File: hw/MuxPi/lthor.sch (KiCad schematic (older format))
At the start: 12 parts, among them J4 CONN_01X04, J5 CONN_01X05, Q13 2N7002, Q14 2N7002, Q15 BSO130P03S, Q16 IRLML2246TRPBF, U13 TS3USB30EDGSR

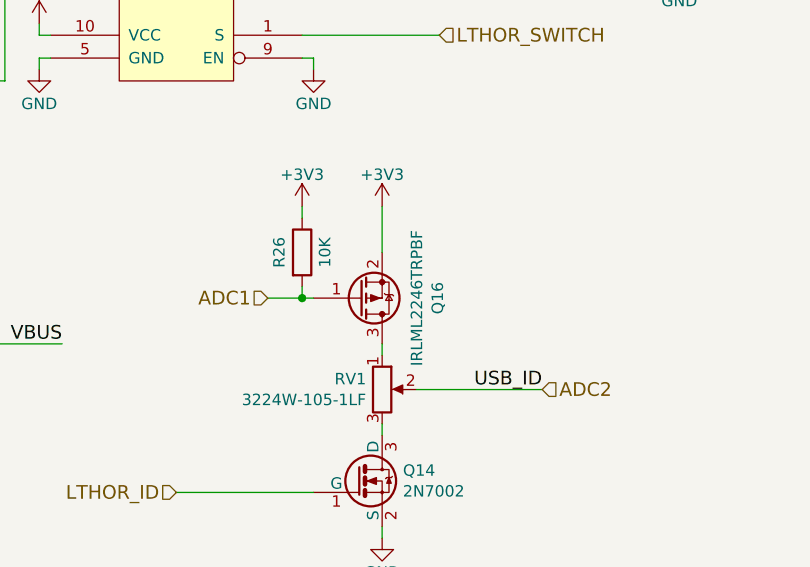
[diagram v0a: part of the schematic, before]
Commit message: Add detailed info to MuxPi electronic components
The additional information includes manufacturer names and
manufacturer symbols for all components except ceramic capacitors
and resistors. It allows to create BOM (Bill Of Materials) with
actual product names.

Change-Id: Id1c518bba60322d4b8b132ad14261806070abc27
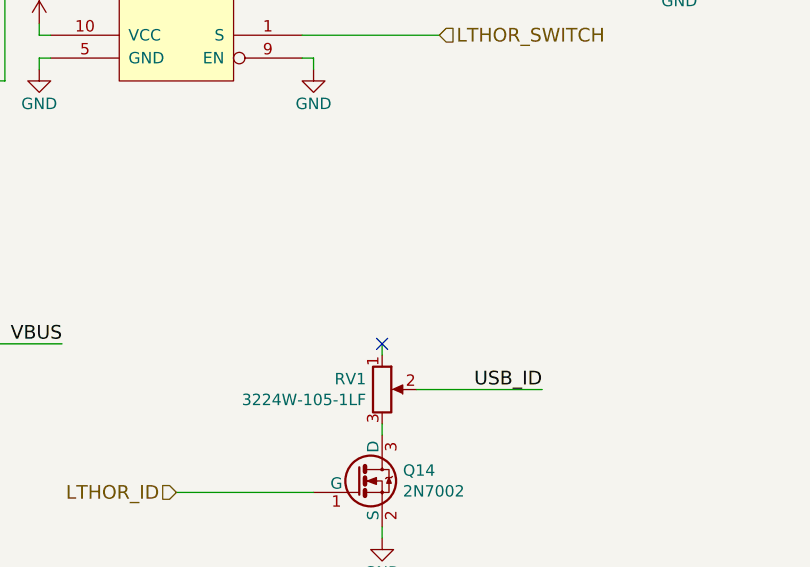
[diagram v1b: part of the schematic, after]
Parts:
- removed Q16: IRLML2246TRPBF, TO_SOT_Packages_SMD:SOT-23, symbol MuxPi:Q_PMOS_GSD
- removed R26: 10K, Resistors_SMD:R_0805, symbol MuxPi:R
- J4: Manufacturer (none) -> CONNFLY; Symbol (none) -> DS1065-01-1*4S8BV
- Q13, Q14: Manufacturer (none) -> ON SEMICONDUCTOR (FAIRCHILD); Symbol (none) -> 2N7002
- Q15: Manufacturer (none) -> INFINEON TECHNOLOGIES; Symbol (none) -> BSO130P03SHXUMA1
- RV1: Manufacturer (none) -> ALLCONNE; Symbol (none) -> POT53W105
- U13: Manufacturer (none) -> TEXAS INSTRUMENTS; Symbol (none) -> TS3USB30EDGSR
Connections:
- net ADC2 renamed USB_ID
- no-connect marks 1 -> 2
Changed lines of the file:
@@
 F 3 "http://www.tme.eu/pl/Document/cb34e048abb83f790f0df461315a2ac0/DS1065-01.pdf" H 4300 2550 50  0001 C CNN
 F 4 "http://www.tme.eu/pl/details/ds1065-01-1x4s8bv/listwy-i-gniazda-kolkowe/connfly/ds1065-01-1_4s8bv/" H 4300 2550 60  0001 C CNN "Shop link"
+F 5 "CONNFLY" H 4300 2550 50  0001 C CNN "Manufacturer"
+F 6 "DS1065-01-1*4S8BV" H 4300 2550 50  0001 C CNN "Symbol"
 	1    4300 2550
 	-1   0    0    -1
@@
 F 3 "http://www.ti.com/lit/ds/symlink/ts3usb30e.pdf" H 3690 1790 60  0001 C CNN
 F 4 "http://pl.farnell.com/texas-instruments/ts3usb30edgsr/multiplexer-demultiplexer-1-2/dp/2335701" H 5900 2900 60  0001 C CNN "Shop link"
+F 5 "TEXAS INSTRUMENTS" H 5900 2900 50  0001 C CNN "Manufacturer"
+F 6 "TS3USB30EDGSR" H 5900 2900 50  0001 C CNN "Symbol"
 	1    5900 2900
 	-1   0    0    -1
@@
 VBUS
 $Comp
-L MuxPi:2N7002 Q14
-U 1 1 58DAC98F
-P 6700 5200
-F 0 "Q14" H 6891 5246 50  0000 L CNN
-F 1 "2N7002" H 6891 5155 50  0000 L CNN
-F 2 "TO_SOT_Packages_SMD:SOT-23" H 6900 5125 50  0001 L CIN
-F 3 "https://www.nxp.com/documents/data_sheet/2N7002.pdf" H 6700 5200 50  0001 L CNN
-F 4 "http://www.tme.eu/pl/details/2n7002/tranzystory-z-kanalem-n-smd/fairchild-semiconductor/" H 6700 5200 60  0001 C CNN "Shop link"
-	1    6700 5200
-	1    0    0    -1
-$EndComp
-$Comp
 L MuxPi:GND #PWR0200
 U 1 1 58DAC996
@@
 F 3 "https://www.maritex.com.pl/product/attachment/37649/pot-53w.pdf" H 6800 4800 50  0001 C CNN
 F 4 "https://www.maritex.com.pl/elementy_pasywne/potencjometry/wieloobrotowe/wieloobrotowe_smd/potencjometry_precyzyjne_wieloobrotowe_smd/pot53w105.html" H 6800 4800 60  0001 C CNN "Shop link"
+F 5 "ALLCONNE" H 6800 4800 50  0001 C CNN "Manufacturer"
+F 6 "POT53W105" H 6800 4800 50  0001 C CNN "Symbol"
 	1    6800 4800
 	1    0    0    -1
@@
 F 3 "" H 3300 5650 60  0000 C CNN
 	1    3300 5650
-	1    0    0    -1
-$EndComp
-$Comp
-L MuxPi:BSO130P03S Q15
-U 1 1 58DAF6B4
-P 4500 4800
-F 0 "Q15" H 4500 5307 50  0000 C CNN
-F 1 "BSO130P03S" H 4500 5216 50  0000 C CNN
-F 2 "mux-footprints:SOIC-8" H 4500 5125 50  0001 C CIN
-F 3 "http://www.tme.eu/pl/Document/fde90035d9a6021d44d09086b0d9119c/BSO130P03SHXUMA1-DTE.pdf" V 4500 4800 50  0001 L CNN
-F 4 "http://www.tme.eu/pl/details/bso130p03shxuma1/tranzystory-z-kanalem-p-smd/infineon-technologies/" H 4500 4800 60  0001 C CNN "Shop link"
-	1    4500 4800
-	1    0    0    -1
-$EndComp
-$Comp
-L MuxPi:2N7002 Q13
-U 1 1 58DAF6BD
-P 3750 5200
-F 0 "Q13" H 3941 5246 50  0000 L CNN
-F 1 "2N7002" H 3941 5155 50  0000 L CNN
-F 2 "TO_SOT_Packages_SMD:SOT-23" H 3950 5125 50  0001 L CIN
-F 3 "https://www.nxp.com/documents/data_sheet/2N7002.pdf" H 3750 5200 50  0001 L CNN
-F 4 "http://www.tme.eu/pl/details/2n7002/tranzystory-z-kanalem-n-smd/fairchild-semiconductor/" H 3750 5200 60  0001 C CNN "Shop link"
-	1    3750 5200
 	1    0    0    -1
 $EndComp
@@
 Text HLabel 7050 3250 2    60   Input ~ 0
 LTHOR_SWITCH
-$Comp
-L MuxPi:Q_PMOS_GSD Q16
-U 1 1 58DB6E6E
-P 6700 4400
-F 0 "Q16" V 7043 4400 50  0000 C CNN
-F 1 "IRLML2246TRPBF" V 6952 4400 50  0000 C CNN
-F 2 "TO_SOT_Packages_SMD:SOT-23" H 6900 4500 50  0001 C CNN
-F 3 "http://www.tme.eu/pl/Document/2f0f749c8d8f8ba613dc3956fc89a382/irlml2246pbf.pdf" H 6700 4400 50  0001 C CNN
-F 4 "http://www.tme.eu/pl/details/irlml2246trpbf/tranzystory-z-kanalem-p-smd/infineon-irf/" V 6700 4400 60  0001 C CNN "Shop link"
-	1    6700 4400
-	1    0    0    1
-$EndComp
-$Comp
-L MuxPi:+3V3 #PWR199
-U 1 1 58DBC567
-P 6800 4000
-AR Path="/58DBC567" Ref="#PWR199"  Part="1"
-AR Path="/58DA42D9/58DBC567" Ref="#PWR0199"  Part="1"
-F 0 "#PWR0199" H 6800 3850 50  0001 C CNN
-F 1 "+3V3" H 6800 4140 50  0000 C CNN
-F 2 "" H 6800 4000 60  0000 C CNN
-F 3 "" H 6800 4000 60  0000 C CNN
-	1    6800 4000
-	1    0    0    -1
-$EndComp
 Wire Wire Line
 	6800 4600 6800 4650
 Wire Wire Line
-	6800 4000 6800 4200
-Wire Wire Line
-	6500 4400 6450 4400
-Text HLabel 7500 4800 2    60   Input ~ 0
-ADC2
-$Comp
-L MuxPi:R R26
-U 1 1 58DBD856
-P 6450 4200
-F 0 "R26" V 6350 4200 50  0000 C CNN
-F 1 "10K" V 6550 4200 50  0000 C CNN
-F 2 "Resistors_SMD:R_0805" V 6380 4200 30  0001 C CNN
-F 3 "" H 6450 4200 30  0000 C CNN
-F 4 "http://www.tme.eu/pl/details/smd0805-560r/rezystory-smd-0805/royal-ohm/0805s8j0561t5e/" V 6450 4200 60  0001 C CNN "Shop link"
-	1    6450 4200
-	1    0    0    -1
-$EndComp
-$Comp
-L MuxPi:+3V3 #PWR197
-U 1 1 58DBDB73
-P 6450 4000
-AR Path="/58DBDB73" Ref="#PWR197"  Part="1"
-AR Path="/58DA42D9/58DBDB73" Ref="#PWR0197"  Part="1"
-F 0 "#PWR0197" H 6450 3850 50  0001 C CNN
-F 1 "+3V3" H 6450 4140 50  0000 C CNN
-F 2 "" H 6450 4000 60  0000 C CNN
-F 3 "" H 6450 4000 60  0000 C CNN
-	1    6450 4000
-	1    0    0    -1
-$EndComp
-Wire Wire Line
-	6450 4000 6450 4050
-Wire Wire Line
-	6450 4350 6450 4400
-Connection ~ 6450 4400
-Text HLabel 6300 4400 0    60   Input ~ 0
-ADC1
-Wire Wire Line
 	4900 4700 4900 4800
 Wire Wire Line
@@
 Wire Wire Line
 	4900 4600 5400 4600
-Wire Wire Line
-	6450 4400 6300 4400
+$Comp
+L MuxPi:2N7002 Q13
+U 1 1 5A88C1DF
+P 3750 5200
+F 0 "Q13" H 3941 5246 50  0000 L CNN
+F 1 "2N7002" H 3941 5155 50  0000 L CNN
+F 2 "TO_SOT_Packages_SMD:SOT-23" H 3950 5125 50  0001 L CIN
+F 3 "https://www.nxp.com/documents/data_sheet/2N7002.pdf" H 3750 5200 50  0001 L CNN
+F 4 "http://www.tme.eu/pl/details/2n7002/tranzystory-z-kanalem-n-smd/fairchild-semiconductor/" H 3750 5200 60  0001 C CNN "Shop link"
+F 5 "ON SEMICONDUCTOR (FAIRCHILD)" H 3750 5200 50  0001 C CNN "Manufacturer"
+F 6 "2N7002" H 3750 5200 50  0001 C CNN "Symbol"
+	1    3750 5200
+	1    0    0    -1
+$EndComp
+$Comp
+L MuxPi:2N7002 Q14
+U 1 1 5A88D4E8
+P 6700 5200
+F 0 "Q14" H 6891 5246 50  0000 L CNN
+F 1 "2N7002" H 6891 5155 50  0000 L CNN
+F 2 "TO_SOT_Packages_SMD:SOT-23" H 6900 5125 50  0001 L CIN
+F 3 "https://www.nxp.com/documents/data_sheet/2N7002.pdf" H 6700 5200 50  0001 L CNN
+F 4 "http://www.tme.eu/pl/details/2n7002/tranzystory-z-kanalem-n-smd/fairchild-semiconductor/" H 6700 5200 60  0001 C CNN "Shop link"
+F 5 "ON SEMICONDUCTOR (FAIRCHILD)" H 6700 5200 50  0001 C CNN "Manufacturer"
+F 6 "2N7002" H 6700 5200 50  0001 C CNN "Symbol"
+	1    6700 5200
+	1    0    0    -1
+$EndComp
+$Comp
+L MuxPi:BSO130P03S Q15
+U 1 1 5A88DDE3
+P 4500 4800
+F 0 "Q15" H 4500 5307 50  0000 C CNN
+F 1 "BSO130P03S" H 4500 5216 50  0000 C CNN
+F 2 "mux-footprints:SOIC-8" H 4500 5125 50  0001 C CIN
+F 3 "http://www.tme.eu/pl/Document/fde90035d9a6021d44d09086b0d9119c/BSO130P03SHXUMA1-DTE.pdf" V 4500 4800 50  0001 L CNN
+F 4 "http://www.tme.eu/pl/details/bso130p03shxuma1/tranzystory-z-kanalem-p-smd/infineon-technologies/" H 4500 4800 60  0001 C CNN "Shop link"
+F 5 "INFINEON TECHNOLOGIES" H 4500 4800 50  0001 C CNN "Manufacturer"
+F 6 "BSO130P03SHXUMA1" H 4500 4800 50  0001 C CNN "Symbol"
+	1    4500 4800
+	1    0    0    -1
+$EndComp
+NoConn ~ 6800 4600
 $EndSCHEMATC

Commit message: Update  hardware design to version 1.4
Change-Id: I72a4381d8bec5616bc1cfe04dc8a5407141c77d5
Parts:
- removed J4: CONN_01X04, Pin_Headers:Pin_Header_Straight_1x04_Pitch1.27mm, symbol MuxPi:CONN_01X04
- removed J5: CONN_01X05, Pin_Headers:Pin_Header_Straight_1x05_Pitch1.27mm, symbol MuxPi:CONN_01X05
- removed Q15: BSO130P03S, mux-footprints:SOIC-8, symbol MuxPi:BSO130P03S
- added J5: UJ2-MBH-1-SMT-TR, MuxPi:USB_Mini-B_Lumberg_2486_01_Horizontal, symbol Connector:USB_B_Mini
- added Q6: DMP2035U-7, MuxPi:SOT-23, symbol MuxPi:Q_PMOS_GSD
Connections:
- net +5V: now also Q6.2 (S)
- net GND: now also J5.5 (GND)
- net USB_ID: now also J5.4 (ID)
- net VBUS: now also J5.1 (VBUS), Q6.3 (D)
- net at U13.4 (D+): now also J5.3 (D+)
- net at U13.6 (D-): now also J5.2 (D-)
- net at Q13.3 (D), R25.2: now also Q6.1 (G)
- no-connect marks 2 -> 1
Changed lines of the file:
@@
 EESchema Schematic File Version 4
 LIBS:MuxPi-cache
-EELAYER 26 0
+EELAYER 29 0
 EELAYER END
 $Descr A4 11693 8268
@@
 Sheet 12 12
 Title "MuxPi"
-Date "2018-08-14"
-Rev "1.3"
+Date "2018-11-16"
+Rev "1.4"
 Comp "SRPOL"
 Comment1 "Author: Adam Malinowski <a.malinowsk2@partner.samsung.com>"
@@
 Comment4 ""
 $EndDescr
-$Comp
-L MuxPi:CONN_01X04 J4
-U 1 1 58DA650C
-P 4300 2550
-F 0 "J4" H 4378 2591 50  0000 L CNN
-F 1 "CONN_01X04" H 4378 2500 50  0000 L CNN
-F 2 "Pin_Headers:Pin_Header_Straight_1x04_Pitch1.27mm" H 4300 2550 50  0001 C CNN
-F 3 "http://www.tme.eu/pl/Document/cb34e048abb83f790f0df461315a2ac0/DS1065-01.pdf" H 4300 2550 50  0001 C CNN
-F 4 "http://www.tme.eu/pl/details/ds1065-01-1x4s8bv/listwy-i-gniazda-kolkowe/connfly/ds1065-01-1_4s8bv/" H 4300 2550 60  0001 C CNN "Shop link"
-F 5 "CONNFLY" H 4300 2550 50  0001 C CNN "Manufacturer"
-F 6 "DS1065-01-1*4S8BV" H 4300 2550 50  0001 C CNN "Symbol"
-	1    4300 2550
-	-1   0    0    -1
-$EndComp
 $Comp
 L MuxPi:GND #PWR0196
@@
 	-1   0    0    -1
 $EndComp
-$Comp
-L MuxPi:GND #PWR0194
-U 1 1 58DA8D5B
-P 4550 2750
-F 0 "#PWR0194" H 4550 2500 50  0001 C CNN
-F 1 "GND" H 4550 2600 50  0000 C CNN
-F 2 "" H 4550 2750 60  0000 C CNN
-F 3 "" H 4550 2750 60  0000 C CNN
-	1    4550 2750
-	-1   0    0    -1
-$EndComp
-Text Label 5150 2500 2    60   ~ 0
-USB_LTHOR-
-Text Label 5150 2600 2    60   ~ 0
-USB_LTHOR+
-NoConn ~ 4500 2400
 $Comp
 L MuxPi:TS3USB30EDGSR U13
@@
 	-1   0    0    -1
 $EndComp
-Text Label 7750 2700 0    60   ~ 0
+Text Label 7750 2900 0    60   ~ 0
 USB_ID
 $Comp
 L MuxPi:GND #PWR0201
 U 1 1 58DAB56F
-P 8100 2950
-F 0 "#PWR0201" H 8100 2700 50  0001 C CNN
-F 1 "GND" H 8100 2800 50  0000 C CNN
-F 2 "" H 8100 2950 60  0000 C CNN
-F 3 "" H 8100 2950 60  0000 C CNN
-	1    8100 2950
-	-1   0    0    -1
-$EndComp
-$Comp
-L MuxPi:CONN_01X05 J5
-U 1 1 58DAB6A7
-P 8350 2700
-F 0 "J5" H 8428 2741 50  0000 L CNN
-F 1 "CONN_01X05" H 8428 2650 50  0000 L CNN
-F 2 "Pin_Headers:Pin_Header_Straight_1x05_Pitch1.27mm" H 8350 2700 50  0001 C CNN
-F 3 "" H 8350 2700 50  0001 C CNN
-	1    8350 2700
-	1    0    0    -1
-$EndComp
-Text Label 7750 2800 0    60   ~ 0
+P 8450 3150
+F 0 "#PWR0201" H 8450 2900 50  0001 C CNN
+F 1 "GND" H 8450 3000 50  0000 C CNN
+F 2 "" H 8450 3150 60  0000 C CNN
+F 3 "" H 8450 3150 60  0000 C CNN
+	1    8450 3150
+	-1   0    0    -1
+$EndComp
+Text Label 7750 2500 0    60   ~ 0
 VBUS
 $Comp
@@
 L MuxPi:+5V #PWR0193
 U 1 1 58DB0303
-P 4100 4500
-F 0 "#PWR0193" H 4100 4350 50  0001 C CNN
-F 1 "+5V" H 4115 4673 50  0000 C CNN
-F 2 "" H 4100 4500 50  0000 C CNN
-F 3 "" H 4100 4500 50  0000 C CNN
-	1    4100 4500
+P 4500 4500
+F 0 "#PWR0193" H 4500 4350 50  0001 C CNN
+F 1 "+5V" H 4515 4673 50  0000 C CNN
+F 2 "" H 4500 4500 50  0000 C CNN
+F 3 "" H 4500 4500 50  0000 C CNN
+	1    4500 4500
 	1    0    0    -1
 $EndComp
@@
 	1    0    0    -1
 $EndComp
-Text Label 5400 4600 2    60   ~ 0
+Text Label 5000 5350 2    60   ~ 0
 VBUS
 Wire Wire Line
 	4500 2500 5350 2500
 Wire Wire Line
-	4500 2700 4550 2700
-Wire Wire Line
-	4550 2700 4550 2750
-Wire Wire Line
 	5350 3350 5300 3350
 Wire Wire Line
@@
 	6450 3250 7050 3250
 Wire Wire Line
-	6450 2500 8150 2500
-Wire Wire Line
-	6450 2800 6500 2800
-Wire Wire Line
-	6500 2800 6500 2600
-Wire Wire Line
-	6500 2600 8150 2600
-Wire Wire Line
-	8150 2700 7750 2700
-Wire Wire Line
-	8150 2900 8100 2900
-Wire Wire Line
-	8100 2900 8100 2950
-Wire Wire Line
-	8150 2800 7750 2800
+	6450 2500 6600 2500
+Wire Wire Line
+	8150 2900 7750 2900
+Wire Wire Line
+	8150 2500 7750 2500
 Wire Wire Line
 	6800 5400 6800 5450
@@
 	6950 4800 7500 4800
 Wire Wire Line
-	4800 4600 4900 4600
-Wire Wire Line
-	4800 4700 4900 4700
-Connection ~ 4900 4700
-Wire Wire Line
-	4900 4800 4800 4800
-Connection ~ 4900 4800
-Wire Wire Line
-	4900 4900 4800 4900
-Wire Wire Line
 	3300 5250 3300 5300
-Wire Wire Line
-	4100 4800 4200 4800
-Wire Wire Line
-	4100 4500 4100 4600
-Wire Wire Line
-	4200 4700 4100 4700
-Connection ~ 4100 4700
 Connection ~ 3300 5250
 Wire Wire Line
@@
 Wire Wire Line
 	2750 5250 3300 5250
-Connection ~ 4100 4600
-Wire Wire Line
-	4900 4600 4900 4700
-Connection ~ 4900 4600
 Wire Wire Line
 	3300 5600 3300 5650
 Wire Wire Line
 	3850 5400 3850 5650
-Wire Wire Line
-	4100 4600 4200 4600
 Wire Wire Line
 	3850 4500 3850 4550
@@
 	6800 4600 6800 4650
 Wire Wire Line
-	4900 4700 4900 4800
-Wire Wire Line
-	4900 4800 4900 4900
-Wire Wire Line
-	4100 4700 4100 4800
-Wire Wire Line
 	3300 5250 3550 5250
 Wire Wire Line
 	3850 4950 3850 5000
 Wire Wire Line
-	4100 4600 4100 4700
-Wire Wire Line
-	4900 4600 5400 4600
+	4500 5350 5000 5350
 $Comp
 L MuxPi:2N7002 Q13
@@
 	1    0    0    -1
 $EndComp
-$Comp
-L MuxPi:BSO130P03S Q15
-U 1 1 5A88DDE3
-P 4500 4800
-F 0 "Q15" H 4500 5307 50  0000 C CNN
-F 1 "BSO130P03S" H 4500 5216 50  0000 C CNN
-F 2 "mux-footprints:SOIC-8" H 4500 5125 50  0001 C CIN
-F 3 "http://www.tme.eu/pl/Document/fde90035d9a6021d44d09086b0d9119c/BSO130P03SHXUMA1-DTE.pdf" V 4500 4800 50  0001 L CNN
-F 4 "http://www.tme.eu/pl/details/bso130p03shxuma1/tranzystory-z-kanalem-p-smd/infineon-technologies/" H 4500 4800 60  0001 C CNN "Shop link"
-F 5 "INFINEON TECHNOLOGIES" H 4500 4800 50  0001 C CNN "Manufacturer"
-F 6 "BSO130P03SHXUMA1" H 4500 4800 50  0001 C CNN "Symbol"
-	1    4500 4800
-	1    0    0    -1
-$EndComp
 NoConn ~ 6800 4600
+$Comp
+L MuxPi:Q_PMOS_GSD Q6
+U 1 1 5C2D9E97
+P 4400 4950
+F 0 "Q6" H 4606 4996 50  0000 L CNN
+F 1 "DMP2035U-7" H 4606 4905 50  0000 L CNN
+F 2 "MuxPi:SOT-23" H 4600 5050 50  0001 C CNN
+F 3 "https://www.tme.eu/pl/Document/c0089df8c5de3ea3a074034d05f63960/DMP2035U.pdf" H 4400 4950 50  0001 C CNN
+F 4 "DMP2035U-7" H 4400 4950 50  0001 C CNN "Symbol"
+F 5 "DIODES INCORPORATED" H 4400 4950 50  0001 C CNN "Manufacturer"
+	1    4400 4950
+	1    0    0    1
+$EndComp
+Wire Wire Line
+	4500 4500 4500 4750
+Wire Wire Line
+	4500 5350 4500 5150
+$Comp
+L Connector:USB_B_Mini J5
+U 1 1 5C2DF76E
+P 8450 2700
+F 0 "J5" H 8220 2689 50  0000 R CNN
+F 1 "UJ2-MBH-1-SMT-TR " H 8220 2598 50  0000 R CNN
+F 2 "MuxPi:USB_Mini-B_Lumberg_2486_01_Horizontal" H 8600 2650 50  0001 C CNN
+F 3 "https://pl.mouser.com/datasheet/2/670/uj2-mbh-smt-1313286.pdf" H 8600 2650 50  0001 C CNN
+F 4 "https://pl.mouser.com/ProductDetail/CUI/UJ2-MBH-1-SMT-TR?qs=sGAEpiMZZMulM8LPOQ%252byk%252br6FietFiXBYOK8b9%2fsuNIy0pbKqeLWLA%3d%3d" H 8450 2700 50  0001 C CNN "Shop link"
+F 5 "0.492" H 8450 2700 50  0001 C CNN "Price"
+F 6 "UJ2-MBH-1-SMT-TR " H 8450 2700 50  0001 C CNN "Symbol"
+	1    8450 2700
+	-1   0    0    -1
+$EndComp
+Wire Wire Line
+	8450 3100 8450 3150
+Wire Wire Line
+	7100 2800 8150 2800
+Wire Wire Line
+	6600 2500 6600 2700
+Wire Wire Line
+	6600 2700 6950 2700
+Wire Wire Line
+	6450 2800 6950 2800
+Wire Wire Line
+	6950 2800 7100 2700
+Wire Wire Line
+	6950 2700 7100 2800
+Wire Wire Line
+	7100 2700 8150 2700
+Text HLabel 4500 2500 0    60   Input ~ 0
+USB_LTHOR-
+Text HLabel 4500 2600 0    60   Input ~ 0
+USB_LTHOR+
 $EndSCHEMATC
